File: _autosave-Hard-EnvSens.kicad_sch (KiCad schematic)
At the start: 75 parts, among them J1 TYPE-C-31-M-12, J2 Conn_01x04_Socket, J3 Conn_02x02_Odd_Even, J4 Conn_01x04_Pin, J5 Conn_02x02_Odd_Even, Q1 SS8050, Q2 SS8050, SW1 SW_Push, SW2 SW_Push, SW3 SW_Push, U1 LD1117S33TR_SOT223, U2 ESP32-C6-WROOM-1, U3 IP5306, U4 VEML7700-TR, U5 DPS368, U6 SGP41-D-R4, U7 SHT40-AD1B-R2, U8 AS7341-DLGT, U9 TPS79318DBVTG4

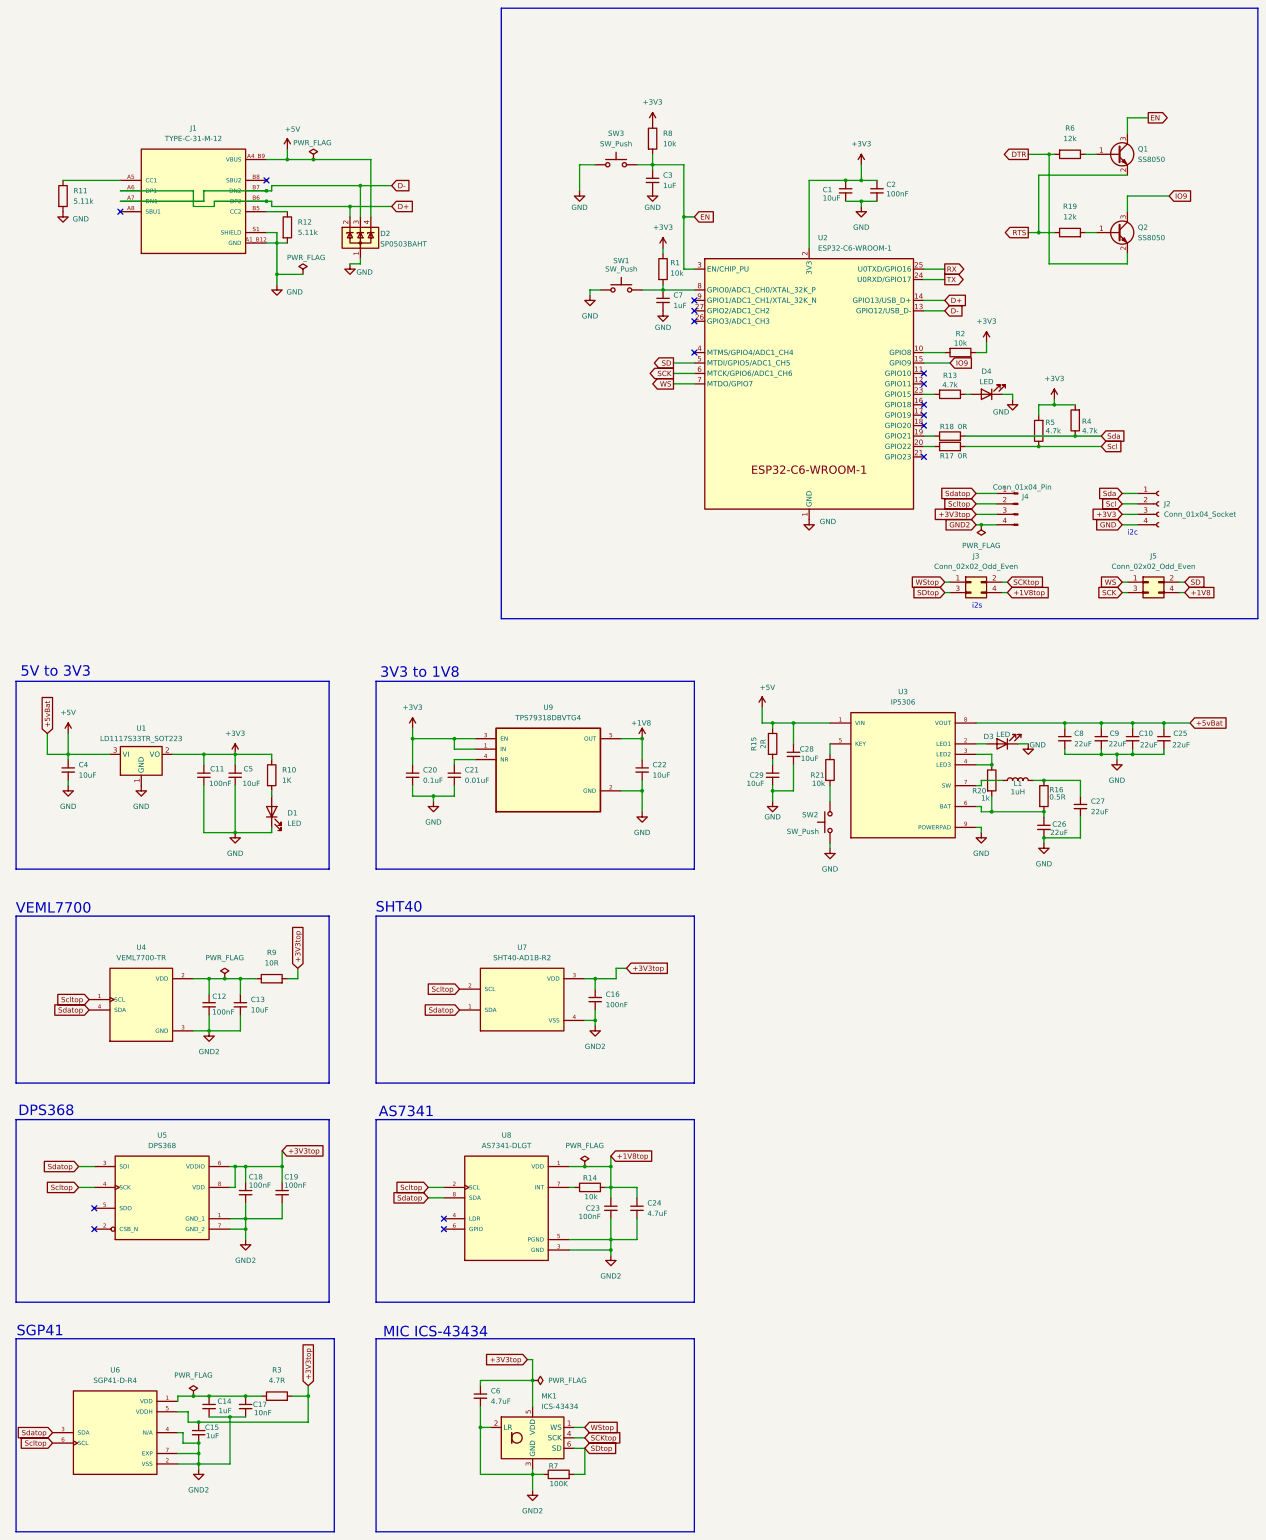
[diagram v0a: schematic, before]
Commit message: Baterry charger + giroscope
Magnetometer not connected
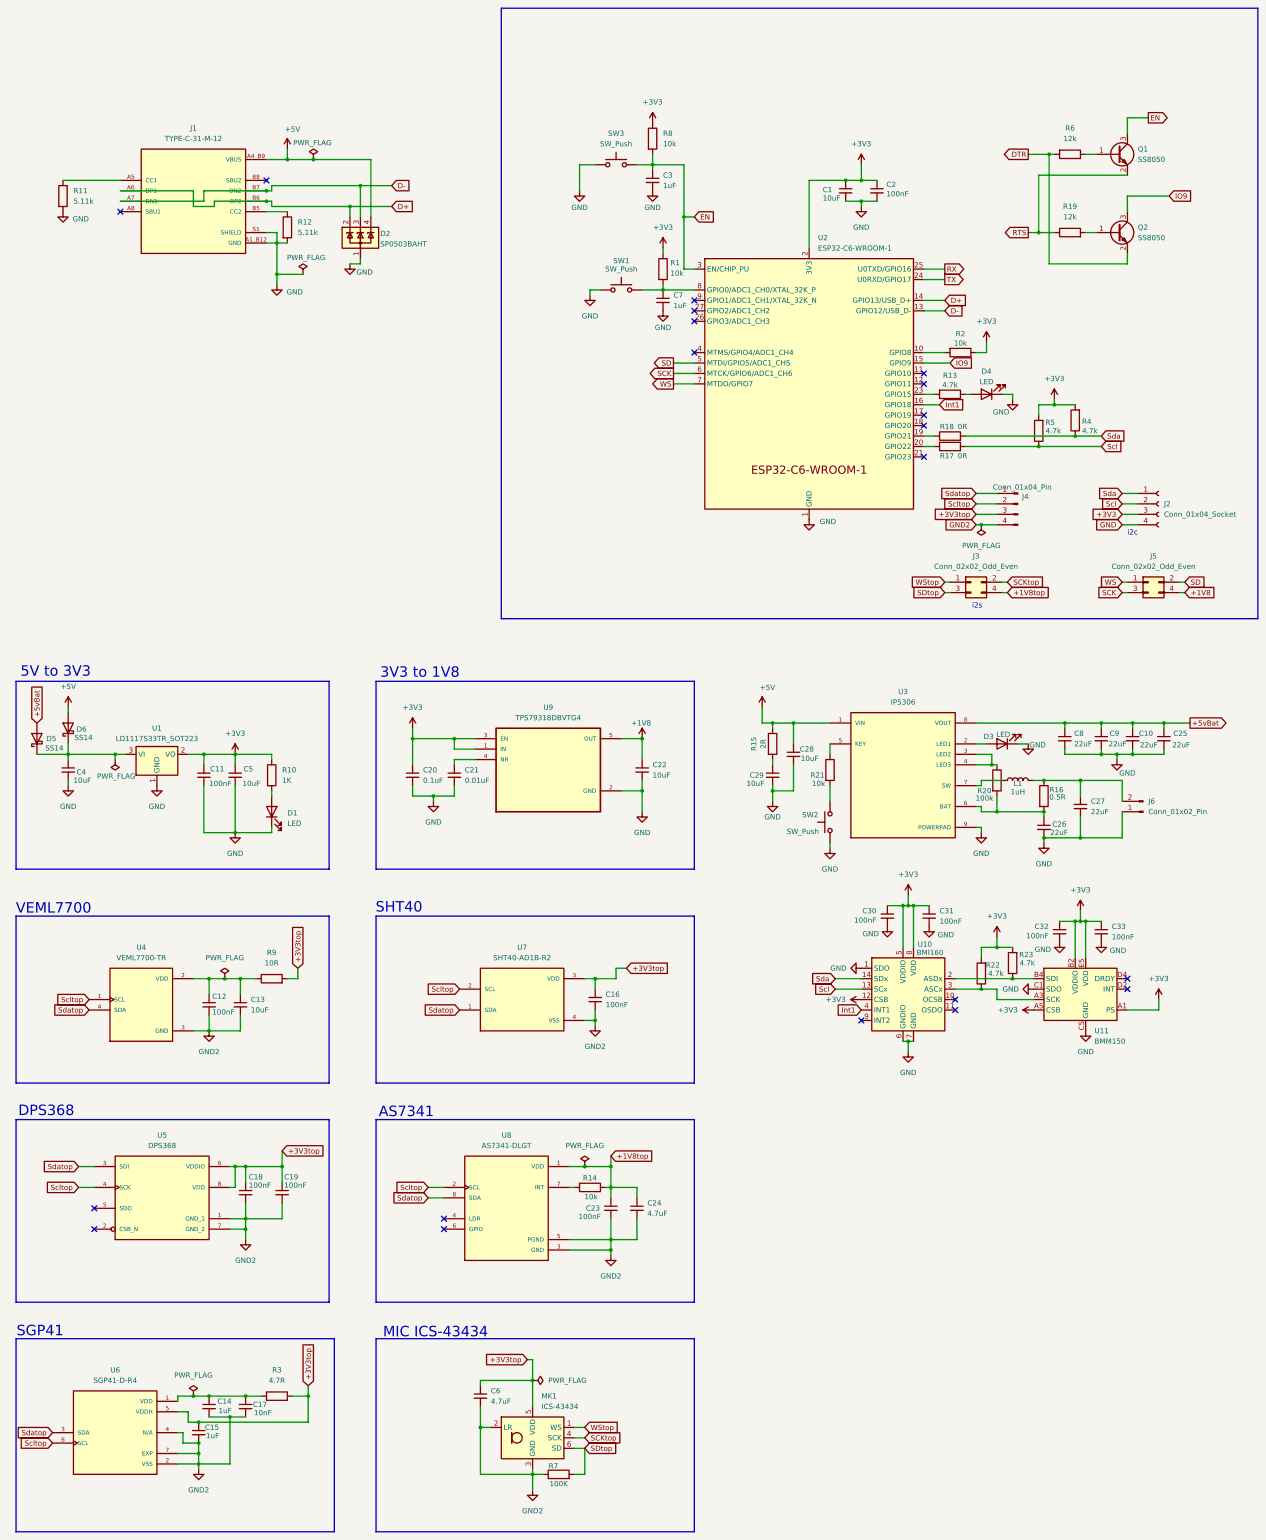
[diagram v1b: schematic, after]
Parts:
- added C30, C31, C32, C33: 100nF, Capacitor_SMD:C_0603_1608Metric, symbol Device:C_Small
- added D5, D6: SS14, Diode_SMD:D_SMA, symbol Diode:SS14
- added J6: Conn_01x02_Pin, Connector_PinHeader_2.54mm:PinHeader_1x02_P2.54mm_Vertical, symbol Connector:Conn_01x02_Pin
- added R22, R23: 4.7k, Resistor_SMD:R_0603_1608Metric, symbol Device:R
- added U10: BMI160, Package_LGA:Bosch_LGA-14_3x2.5mm_P0.5mm, symbol Sensor_Motion:BMI160
- added U11: BMM150, Package_CSP:WLCSP-12_1.56x1.56mm_P0.4mm, symbol Sensor_Magnetic:BMM150
- L1: footprint (none) -> Inductor_SMD:L_TechFuse_SL0630
- R20: value 1k -> 100k
- U3: footprint IP5306:SOP127P600X165-9N -> libs:SOP127P600X165-9N
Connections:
- net +3V3: now also C30.1, C31.1, C32.1, C33.1, R22.2, R23.2, U10.12 (CSB), U10.5 (VDDIO), U10.8 (VDD), U11.A1 (PS), U11.A5 (CSB), U11.B2 (VDDIO), U11.E5 (VDD)
- net +5V: now also D6.2 (A); no longer C10.1, C25.1, C4.1, C8.1, C9.1, U1.3 (VI), U3.8 (VOUT)
- net GND: now also C30.2, C31.2, C32.2, C33.2, J6.1 (Pin_1), U10.1 (SDO), U10.6 (GNDIO), U10.7 (GND), U11.C1 (SDO), U11.C5 (GND), U11.E1 (GND), U11.E3 (GND)
- net Scl: now also U10.13 (SCx)
- net Sda: now also U10.14 (SDx)
- net at C27.1, L1.2, R16.1: now also J6.2 (Pin_2)
- net Int1: now reaches U2.16 (GPIO18)
- net Int1: now also U10.4 (INT1)
- new net: R23.1, U10.2 (ASDx), U11.B4 (SDI)
- new net: R22.1, U10.3 (ASCx), U11.A3 (SCK)
- new net: C4.1, D5.1 (K), D6.1 (K), U1.3 (VI)
- new net +5vBat: C10.1, C25.1, C8.1, C9.1, D5.2 (A), U3.8 (VOUT)
- no-connect marks 16 -> 20
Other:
- moved on the sheet: R20, U1
